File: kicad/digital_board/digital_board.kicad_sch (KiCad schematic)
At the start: 94 parts

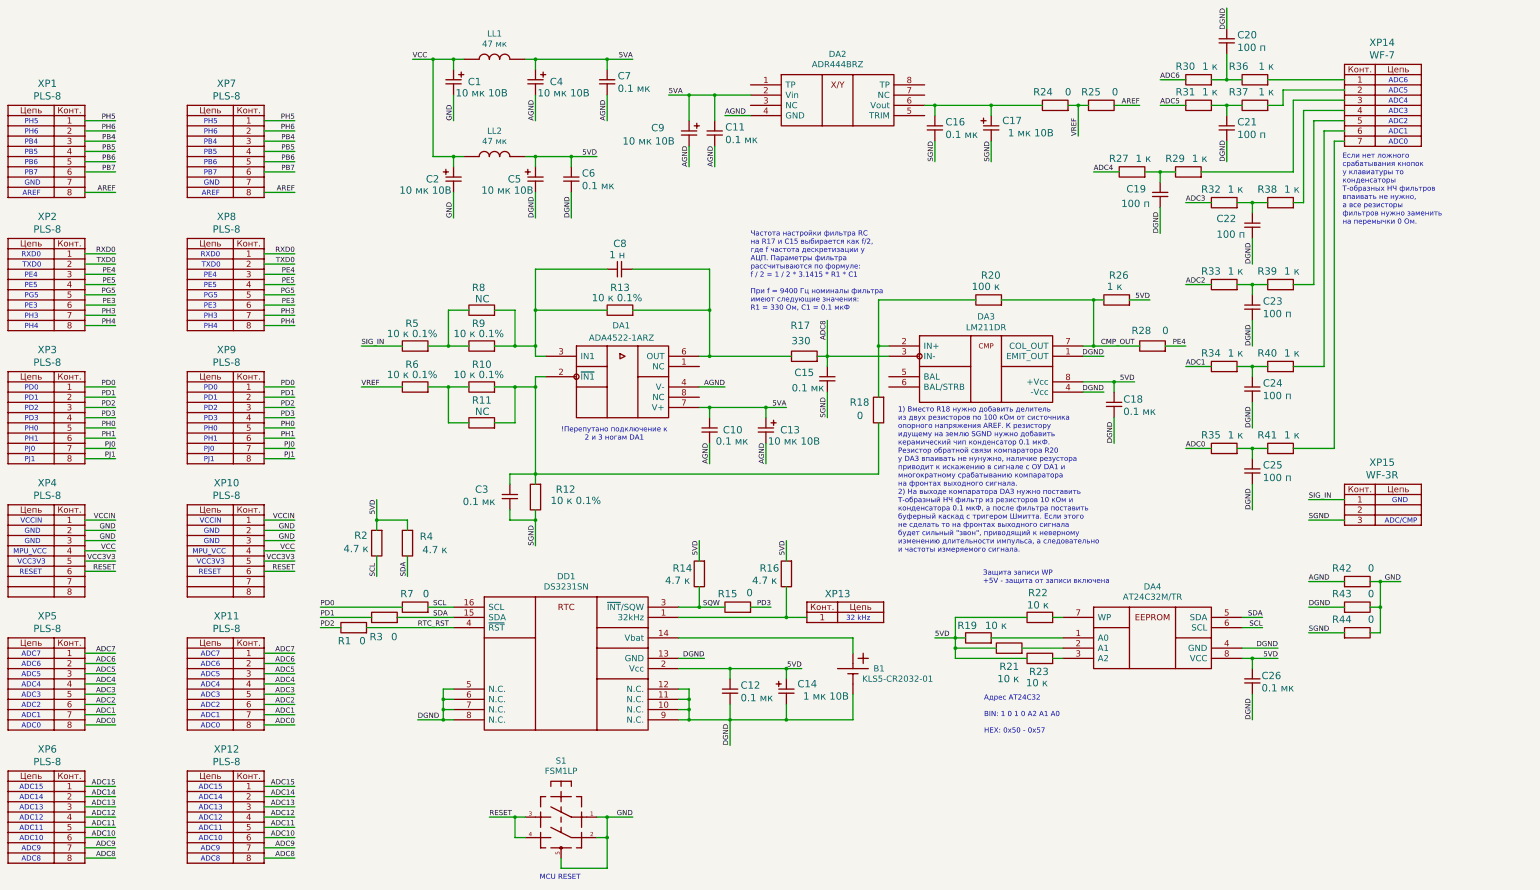
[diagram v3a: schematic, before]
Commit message: Исправил ошибки в схеме и на печатной плате. Увеличил версию цифровой платы до 1.1.
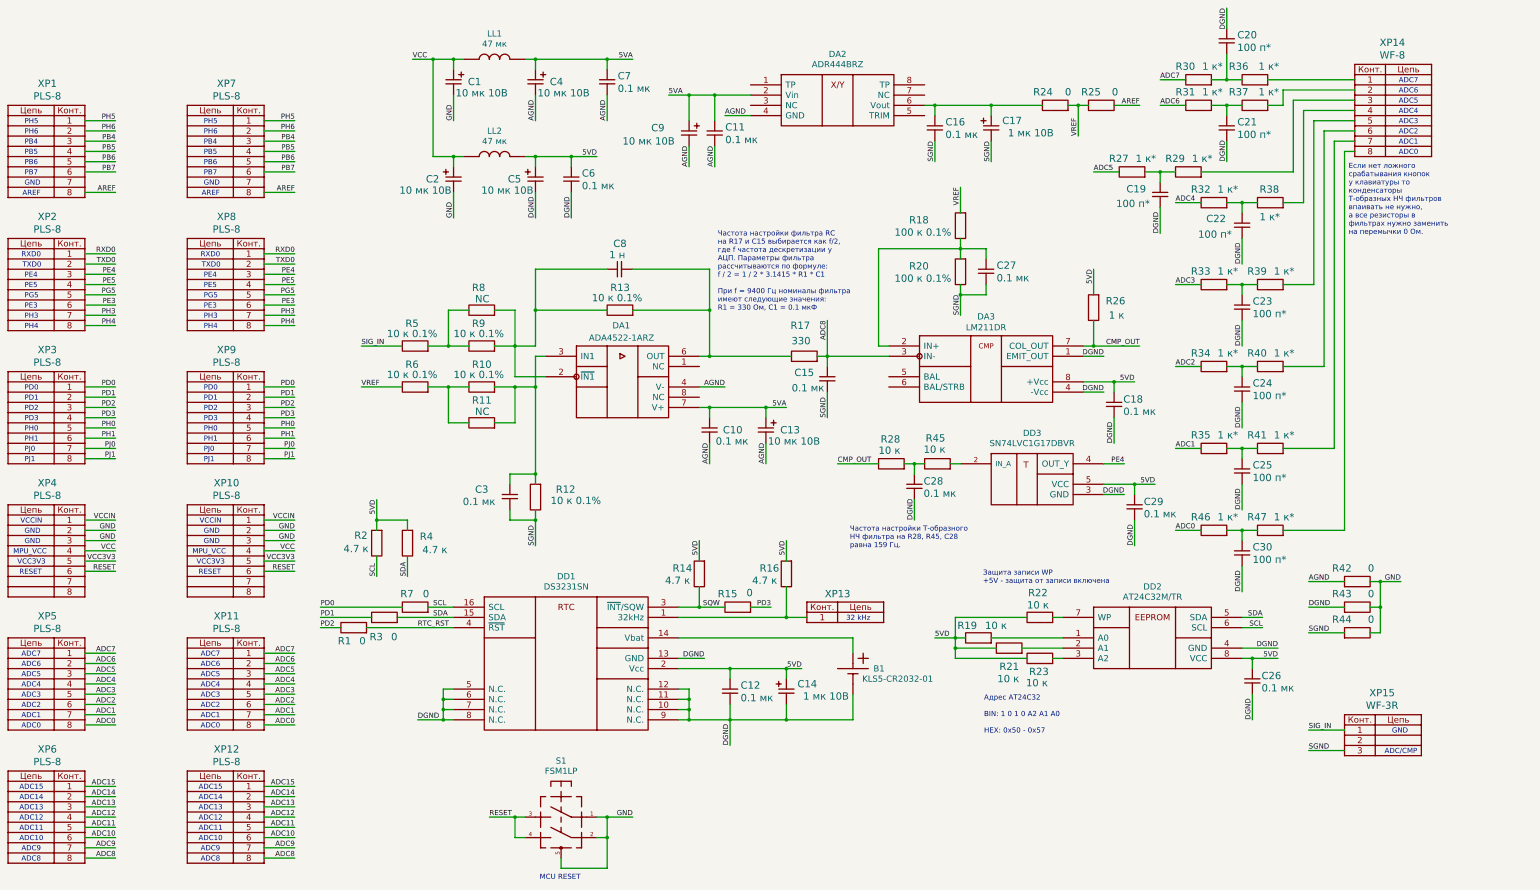
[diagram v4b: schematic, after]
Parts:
- added C27, C28, C29: 0.1 мк, IWsmd_case:SMD0805, symbol LFcapitors:CAPITORS
- added C30: 100 п*, IWsmd_case:SMD0805, symbol LFcapitors:CAPITORS
- added DD3: SN74LVC1G17DBVR, IWsmd_case:SOT753, symbol LFcomponents:74LVC1G17
- added R45: 10 к, IWsmd_case:SMD0805, symbol LFresistor:RESISTOR
- added R46, R47: 1 к*, IWsmd_case:SMD0805, symbol LFresistor:RESISTOR
- C19, C20, C21, C22, C23, C24, C25: value 100 п -> 100 п*
- R18: value 0 -> 100 к 0.1%
- R20: value 100 к -> 100 к 0.1%
- R27, R29, R30, R31, R32, R33, R34, R35, R36, R37, R38, R39, R40, R41: value 1 к -> 1 к*
- R28: value 0 -> 10 к
- XP14: value WF-7 -> WF-8; footprint IWconnectors:WF-7 -> IWconnectors:WF-8; symbol LFconnectors:connector_7pin_gost -> LFconnectors:connector_8pin_gost
- renumbered DA4 to DD2
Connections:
- net 5VD: now also C29.1, DD3.5 (VCC)
- net ADC0: now also R46.2; no longer R35.2
- net ADC1: now also R35.2; no longer R34.2
- net ADC2: now also R34.2; no longer R33.2
- net ADC3: now also R33.2; no longer R32.2
- net ADC4: now also R32.2; no longer R27.2
- net ADC5: now also R27.2; no longer R31.2
- net ADC6: now also R31.2; no longer R30.2
- net ADC7: now also R30.2
- net CMP_OUT: no longer R20.1
- net DGND: now also C28.2, C29.2, C30.2, DD3.3 (GND)
- net PE4: now also DD3.4 (OUT_Y); no longer R28.1
- net SGND: now also R20.2, C27.2
- net VREF: now also R18.1
- net at C3.1, R10.1, R11.1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: now also DA1.3 (IN1); no longer DA1.2 (~{IN1}), R18.2
- net at C8.1, R13.2, R8.1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: now also DA1.2 (~{IN1}); no longer DA1.3 (IN1)
- new net: C27.1, DA3.2 (IN+), R18.2, R20.1
- new net: R47.1, XP14.8
- new net: C28.1, R28.1, R45.2
- new net: DD3.2 (IN_A), R45.1
- new net: C30.1, R46.1, R47.2
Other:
- note added: "Если нет ложного срабатывания кнопок у клавиатуры то конденсаторы Т-образных НЧ фильтров впаивать не нужно, а все резисторы в фильтрах нужно заменить на перемычки 0 Ом."
- note added: "Частота настройки Т-образного НЧ фильтра на R28, R45, С28 равна 159 Гц."
- note removed: "!Перепутано подключение к 2 и 3 ногам DA1"
- note removed: "1) Вместо R18 нужно добавить делитель из двух резисторов по 100 кОм от систочника опорного напряжения AREF. К резистору идущему на землю SGND нужно добавить керамический чип конденсатор 0.1 мкФ. Резистор обратной связи компаратора R20 у DA3 впаивать не нунужно, наличие резустора приводит к искажению в сигнале с ОУ DA1 и многократному срабатыванию компаратора на фронтах выходного сигнала. 2) На вы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"
- note removed: "Если нет ложного срабатывания кнопок у клавиатуры то конденсаторы Т-образных НЧ фильтров впаивать не нужно, а все резисторы фильтров нужно заменить на перемычки 0 Ом."
- moved on the sheet: C22, C23, C24, C25, R18, R20, R26, R28, R32, R33, R34, R35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
